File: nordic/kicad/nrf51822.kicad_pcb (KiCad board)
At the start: 2 copper layers, 32.1 x 32.1 mm, 19 parts, among them P1 CONN_01X04, P3 CONN_01X01, SW1 SW_Push, U1 BALF-NRF01E3, X1 Crystal

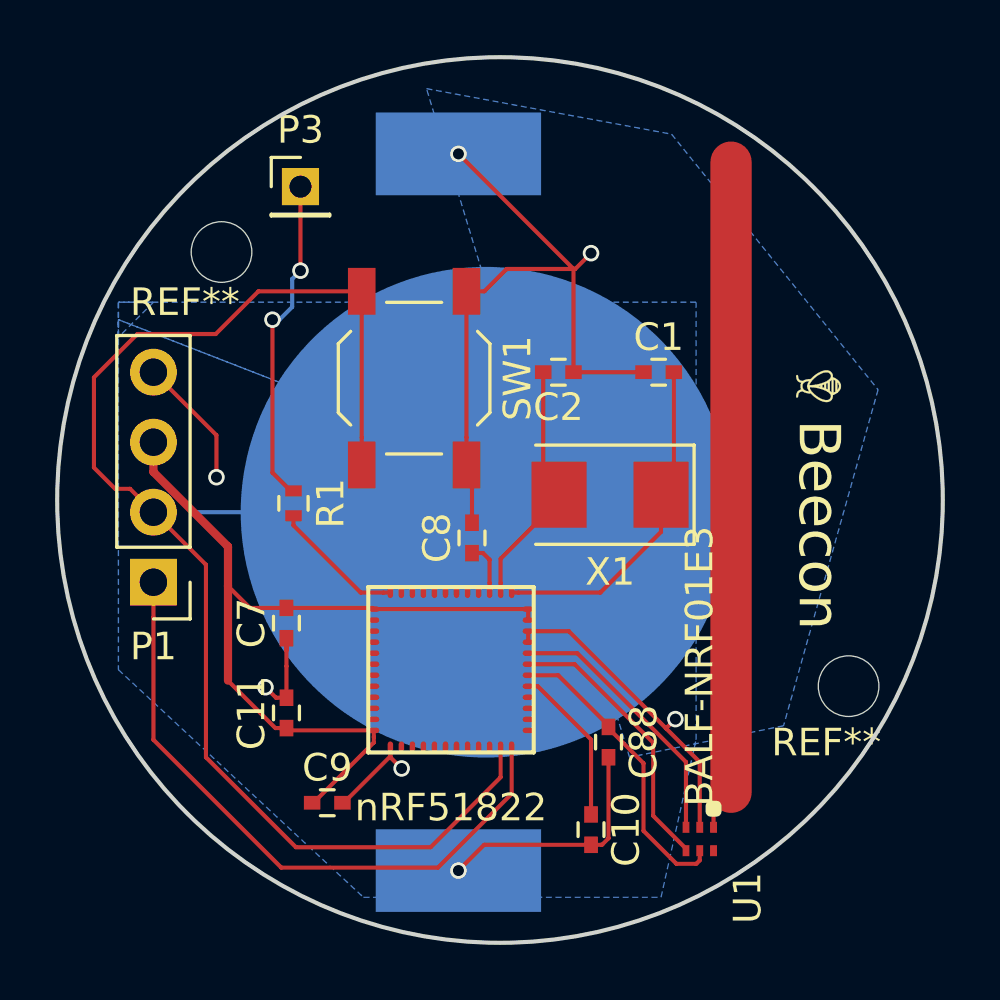
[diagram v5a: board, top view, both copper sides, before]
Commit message: Adicionado componentes 3d no diretório, aumentado a logo e colocado led para teste POST no lugar do botão de reset
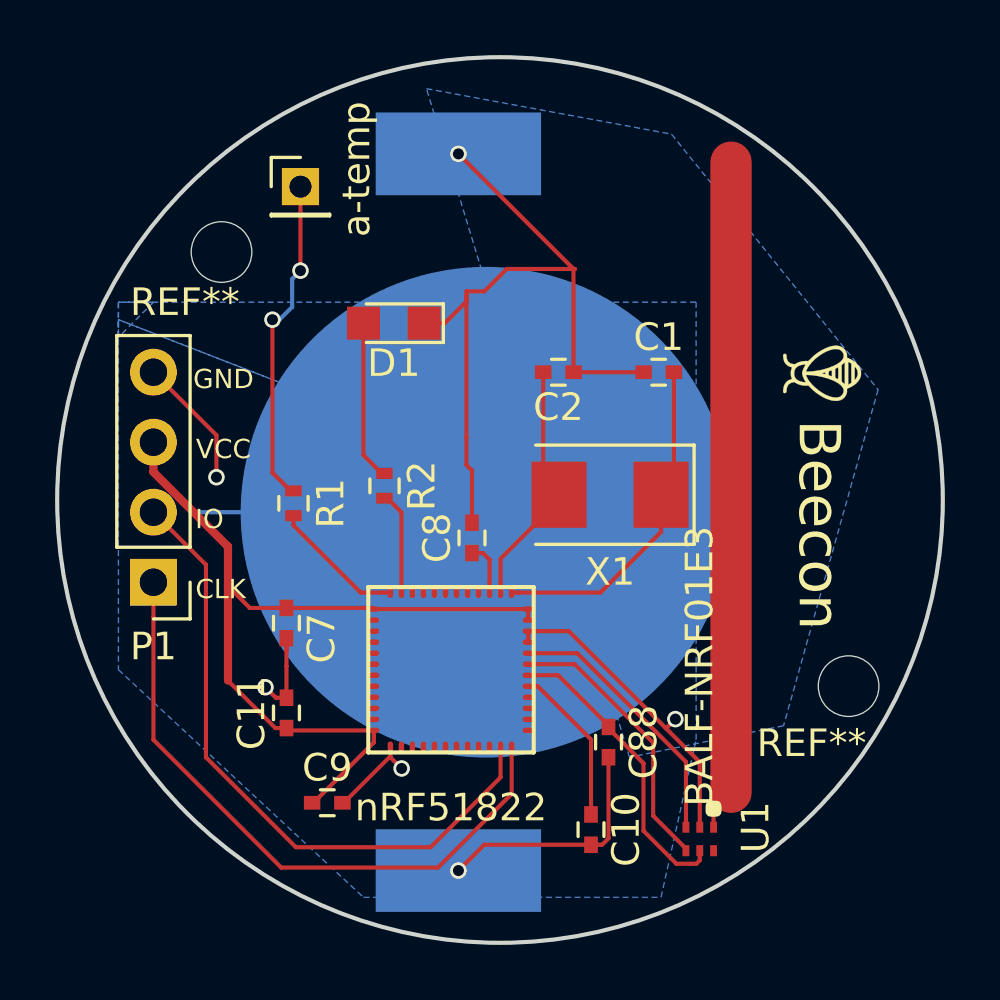
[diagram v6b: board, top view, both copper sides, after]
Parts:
- removed the G*** at (105.4, 118.6)
- removed SW1: SW_Push, Buttons_Switches_SMD:SW_SPST_TL3342
- added D1: LED, LEDs:LED_0805, F.Cu at (90.0, 116.3)
- added G***: LOGO, Pin-Beacon:icon, F.Cu at (105.5, 118.2)
- added R2: R_Small, Resistors_SMD:R_0402, F.Cu at (89.7, 122.2)
- renumbered P3 to a-temp
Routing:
- net Net-(P1-Pad2): track 47.3 -> 23.9 mm
- net Net-(D1-Pad2): track 0.00 -> 5.82 mm
- net Net-(R2-Pad2): track 0.00 -> 3.74 mm
- net GND: track 58.0 -> 59.3 mm, vias 7 -> 6
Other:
- board text added: "CLK"
- board text added: "GND"
- board text added: "IO"
- board text added: "VCC"

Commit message: antena drobradinha
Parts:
- moved G*** 0.89 mm to (106.4, 117.8)
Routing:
- net Net-(AE1-Pad1): track 24.4 -> 25.7 mm
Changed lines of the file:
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@@
-(kicad_pcb (version 4) (host pcbnew 4.0.6)
+(kicad_pcb (version 4) (host pcbnew 4.0.5)
   (general
-    (links 0)
-    (no_connects 2)
+    (links 39)
+    (no_connects 1)
     (area 77.713628 106.607258 109.992372 138.886002)
     (thickness 1.6)
     (drawings 7)
-    (tracks 141)
+    (tracks 143)
     (zones 0)
     (modules 20)
@@
   )
   (module Pin-Beacon:icon (layer F.Cu)
-    (at 105.54 118.15 270)
+    (at 106.3752 117.8306 270)
     (fp_text reference G*** (at 0 0 270) (layer F.SilkS) hide
       (effects (font (thickness 0.3)))
@@
     (arrow2b (pts (xy 112.014 138.938) (xy 111.427579 137.811496)))
   )
-  (gr_text Beecon (at 105.4227 123.6472 270) (layer F.SilkS)
+  (gr_text Beecon (at 106.045 123.063 270) (layer F.SilkS)
     (effects (font (size 1.5 1.5) (thickness 0.3)))
   )
@@
   (segment (start 96.65499 128.305) (end 94.875 128.305) (width 0.15) (layer F.Cu) (net 11) (status 20))
   (segment (start 100.6 134.62) (end 100.6 132.25001) (width 0.15) (layer F.Cu) (net 11) (status 10))
-  (segment (start 102.235 133.35) (end 102.235 110.49) (width 1.5) (layer F.Cu) (net 42))
+  (segment (start 102.235 133.35) (end 103.754933 131.830067) (width 1.5) (layer F.Cu) (net 42))
+  (segment (start 103.754933 131.830067) (end 103.754933 112.009933) (width 1.5) (layer F.Cu) (net 42))
+  (segment (start 103.754933 112.009933) (end 102.235 110.49) (width 1.5) (layer F.Cu) (net 42))
   (segment (start 101.6 133.985) (end 102.235 133.35) (width 0.15) (layer F.Cu) (net 42))
   (segment (start 101.6 134.62) (end 101.6 133.985) (width 0.15) (layer F.Cu) (net 42))
@@
     (polygon
       (pts
-        (xy 91.44 120.65) (xy 80.01 116.205) (xy 80.01 128.905) (xy 88.9 137.16) (xy 99.695 137.16)
-        (xy 100.965 131.445) (xy 100.965 115.57) (xy 80.01 115.57) (xy 80.01 116.84) (xy 80.01 116.205)
+        (xy 100.7872 136.7282) (xy 100.838 108.712) (xy 95.1992 106.9594) (xy 88.265 107.8992) (xy 84.8868 109.6518)
+        (xy 81.407 113.03) (xy 79.3242 116.2558) (xy 78.0796 120.8786) (xy 78.8924 128.143) (xy 80.7974 131.7752)
+        (xy 84.6074 135.6614) (xy 88.3158 137.6426) (xy 89.5604 138.0744) (xy 96.2152 138.3538) (xy 99.2124 137.6426)
       )
     )
-  )
-  (zone (net 2) (net_name GND) (layer B.Cu) (hatch edge 0.508)
-    (connect_pads (clearance 0.508))
-    (min_thickness 0.254)
-    (fill yes (arc_segments 16) (thermal_gap 0.508) (thermal_bridge_width 0.508))
-    (polygon
-      (pts
-        (xy 80.01 116.84) (xy 80.01 115.57) (xy 81.28 115.57)
-      )
-    )
-  )
-  (zone (net 2) (net_name GND) (layer B.Cu) (hatch edge 0.508)
-    (connect_pads (clearance 0.508))
-    (min_thickness 0.254)
-    (fill yes (arc_segments 16) (thermal_gap 0.508) (thermal_bridge_width 0.508))
-    (polygon
-      (pts
-        (xy 91.186 107.823) (xy 100.076 109.474) (xy 107.569 118.745) (xy 104.14 130.937) (xy 98.552 132.08)
-      )
-    )

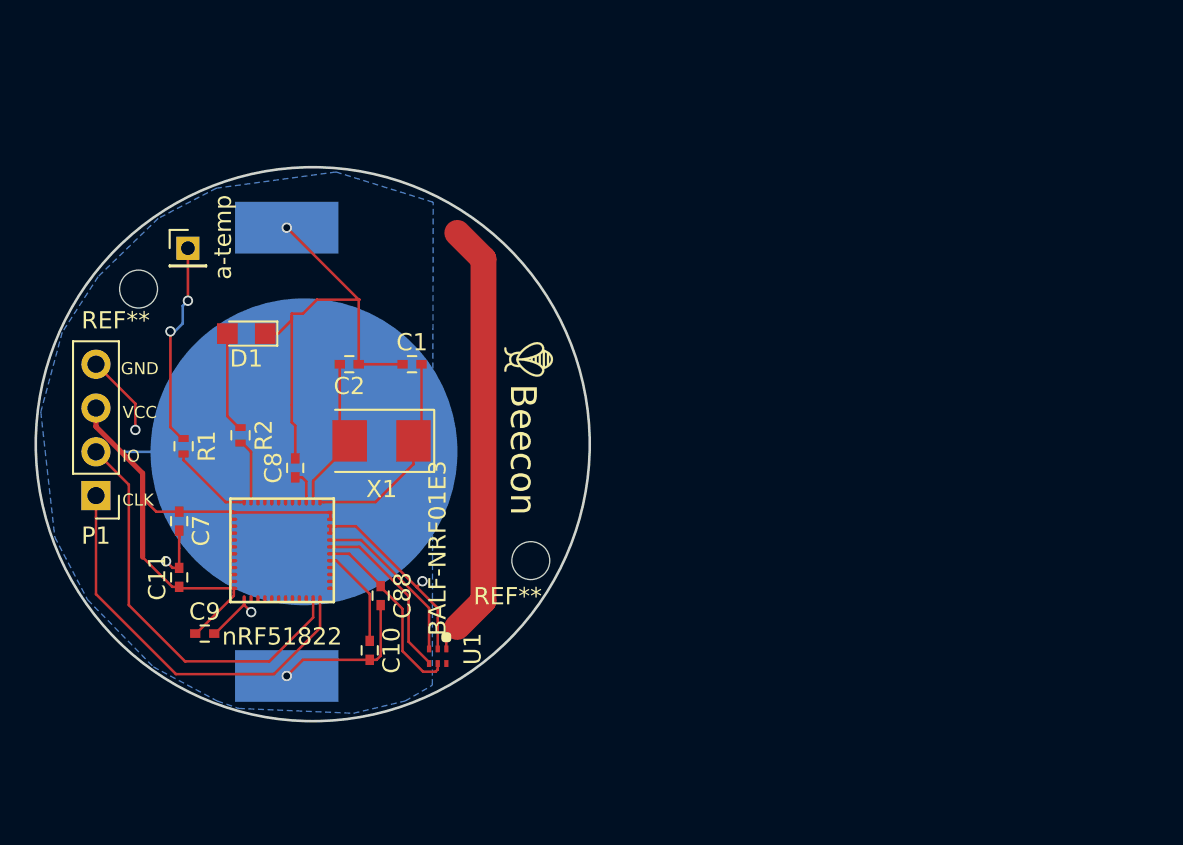
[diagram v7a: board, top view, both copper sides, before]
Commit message: feat(pcb) New Antenna
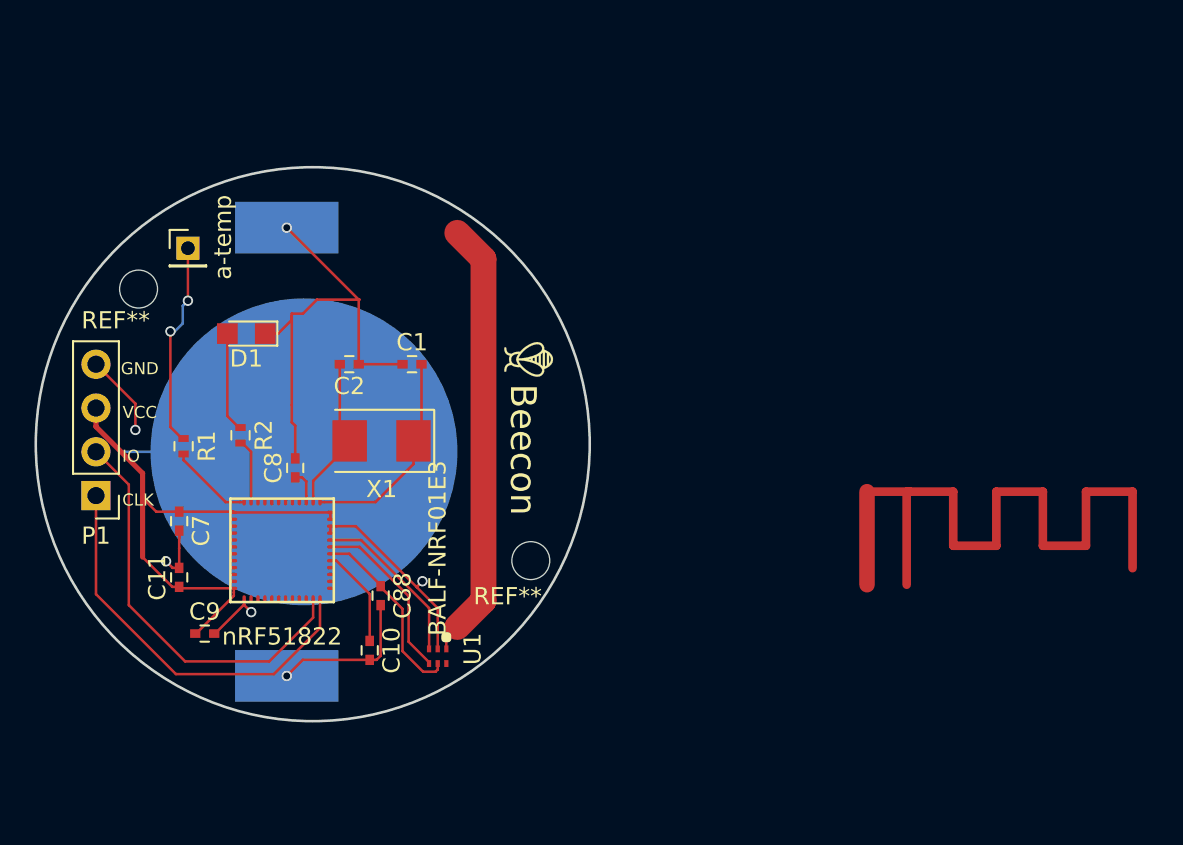
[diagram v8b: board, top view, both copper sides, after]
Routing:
- net (no net): track 0.00 -> 43.2 mm
- removed copper zone on B.Cu, net GND
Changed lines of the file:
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@@
   (general
     (links 39)
-    (no_connects 1)
-    (area 77.713628 106.607258 109.992372 138.886002)
+    (no_connects 6)
+    (area 70.192857 106.607258 141.850002 144.828858)
     (thickness 1.6)
     (drawings 7)
-    (tracks 143)
+    (tracks 156)
     (zones 0)
     (modules 20)
@@
   )
   (gr_circle (center 93.853 122.74663) (end 78.613 127.82663) (layer Edge.Cuts) (width 0.15))
+  (segment (start 128.5 125.5) (end 131 125.5) (width 0.5) (layer F.Cu) (net 0))
+  (segment (start 128.3 125.5) (end 128.3 130.9) (width 0.5) (layer F.Cu) (net 0))
+  (segment (start 126 125.5) (end 128.5 125.5) (width 0.5) (layer F.Cu) (net 0))
+  (segment (start 126 125.5) (end 126 130.9) (width 0.9) (layer F.Cu) (net 0))
+  (segment (start 141.4 125.5) (end 141.4 129.94) (width 0.5) (layer F.Cu) (net 0))
+  (segment (start 138.7 125.5) (end 141.4 125.5) (width 0.5) (layer F.Cu) (net 0))
+  (segment (start 138.7 128.64) (end 138.7 125.5) (width 0.5) (layer F.Cu) (net 0))
+  (segment (start 136.2 128.64) (end 138.7 128.64) (width 0.5) (layer F.Cu) (net 0))
+  (segment (start 136.2 125.5) (end 136.2 128.64) (width 0.5) (layer F.Cu) (net 0))
+  (segment (start 133.5 125.5) (end 136.2 125.5) (width 0.5) (layer F.Cu) (net 0))
+  (segment (start 133.5 128.64) (end 133.5 125.5) (width 0.5) (layer F.Cu) (net 0))
+  (segment (start 131 128.64) (end 133.5 128.64) (width 0.5) (layer F.Cu) (net 0))
+  (segment (start 131 125.5) (end 131 128.64) (width 0.5) (layer F.Cu) (net 0))
   (segment (start 81.28 121.73) (end 81.28 120.65) (width 0.3) (layer F.Cu) (net 1))
   (segment (start 83.9851 125.869804) (end 83.9851 124.4351) (width 0.3) (layer F.Cu) (net 1))
@@
   (segment (start 90.275 123.195) (end 89.762 122.682) (width 0.15) (layer F.Cu) (net 46))
   (segment (start 89.762 122.682) (end 89.662 122.682) (width 0.15) (layer F.Cu) (net 46))
-  (zone (net 2) (net_name GND) (layer B.Cu) (hatch edge 0.508)
-    (connect_pads (clearance 0.508))
-    (min_thickness 0.254)
-    (fill yes (arc_segments 16) (thermal_gap 0.508) (thermal_bridge_width 0.508))
-    (polygon
-      (pts
-        (xy 100.7872 136.7282) (xy 100.838 108.712) (xy 95.1992 106.9594) (xy 88.265 107.8992) (xy 84.8868 109.6518)
-        (xy 81.407 113.03) (xy 79.3242 116.2558) (xy 78.0796 120.8786) (xy 78.8924 128.143) (xy 80.7974 131.7752)
-        (xy 84.6074 135.6614) (xy 88.3158 137.6426) (xy 89.5604 138.0744) (xy 96.2152 138.3538) (xy 99.2124 137.6426)
-      )
-    )
-  )
 )
